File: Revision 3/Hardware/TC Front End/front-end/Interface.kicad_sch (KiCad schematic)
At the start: 18 parts, among them J1 Conn_01x02, J2 4DB-P108-02, J5 Conn_01x04, U1 LM321, U2 LM321, U3 DS18B20+

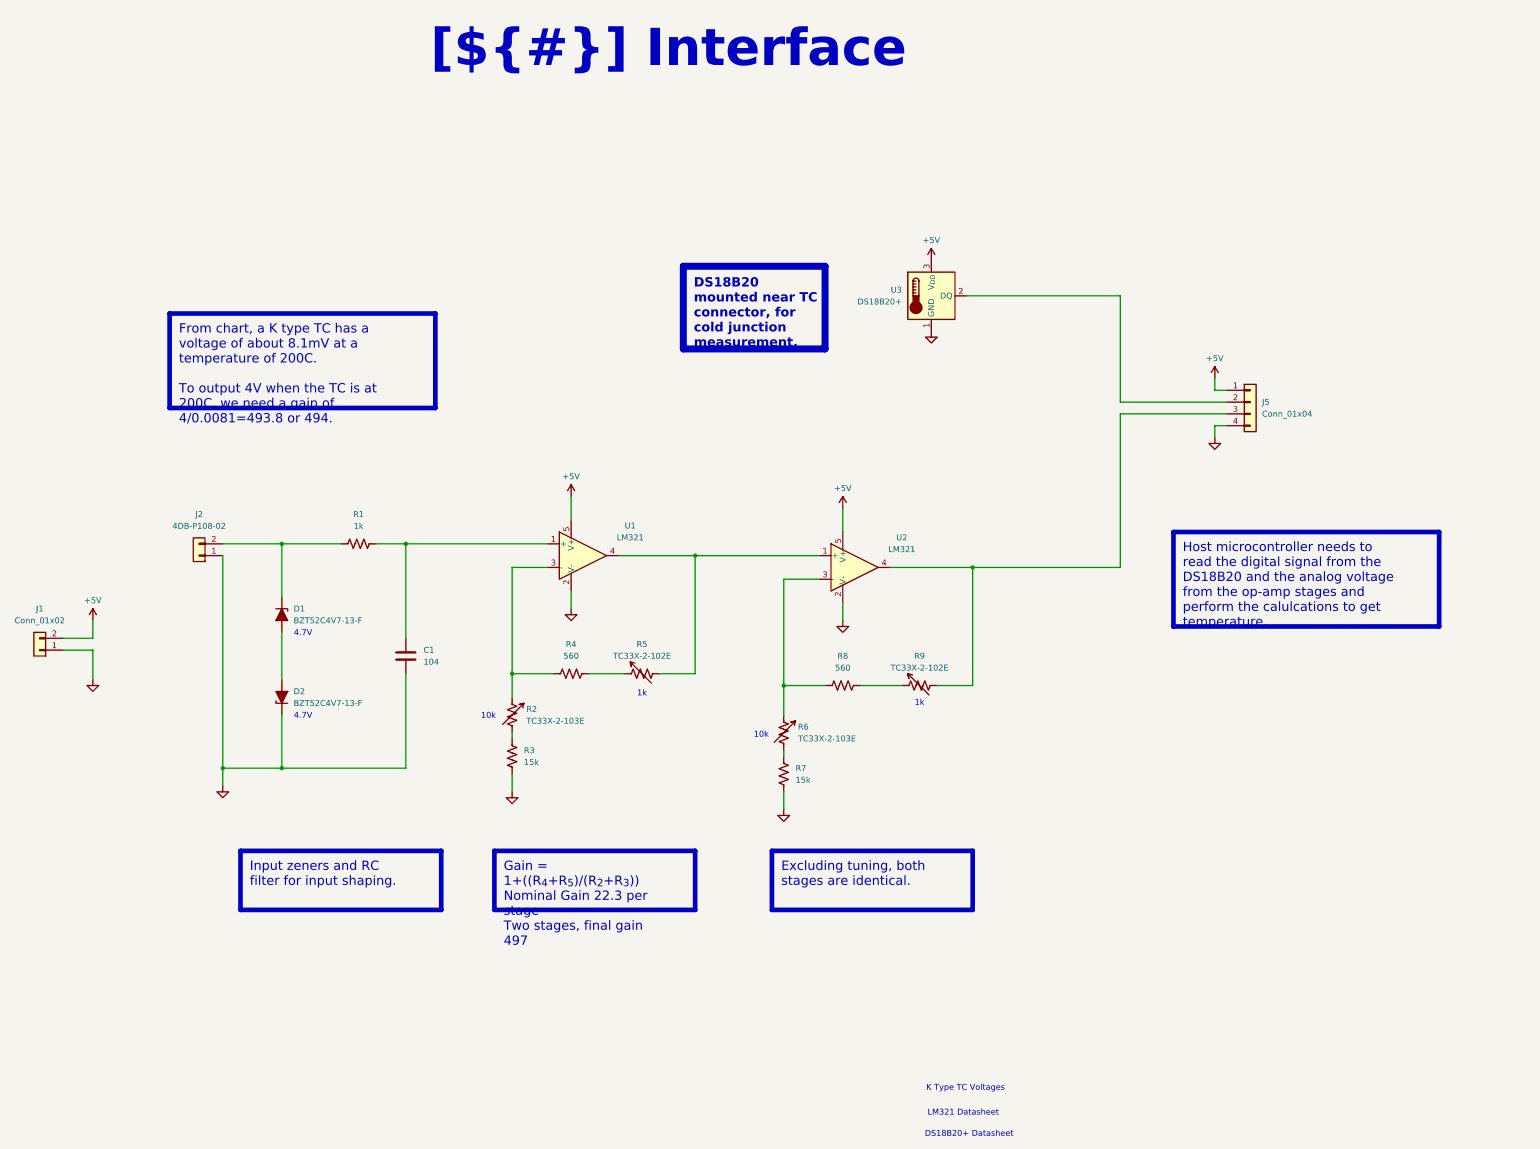
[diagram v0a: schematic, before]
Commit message: PCB layout complete, ready for routing
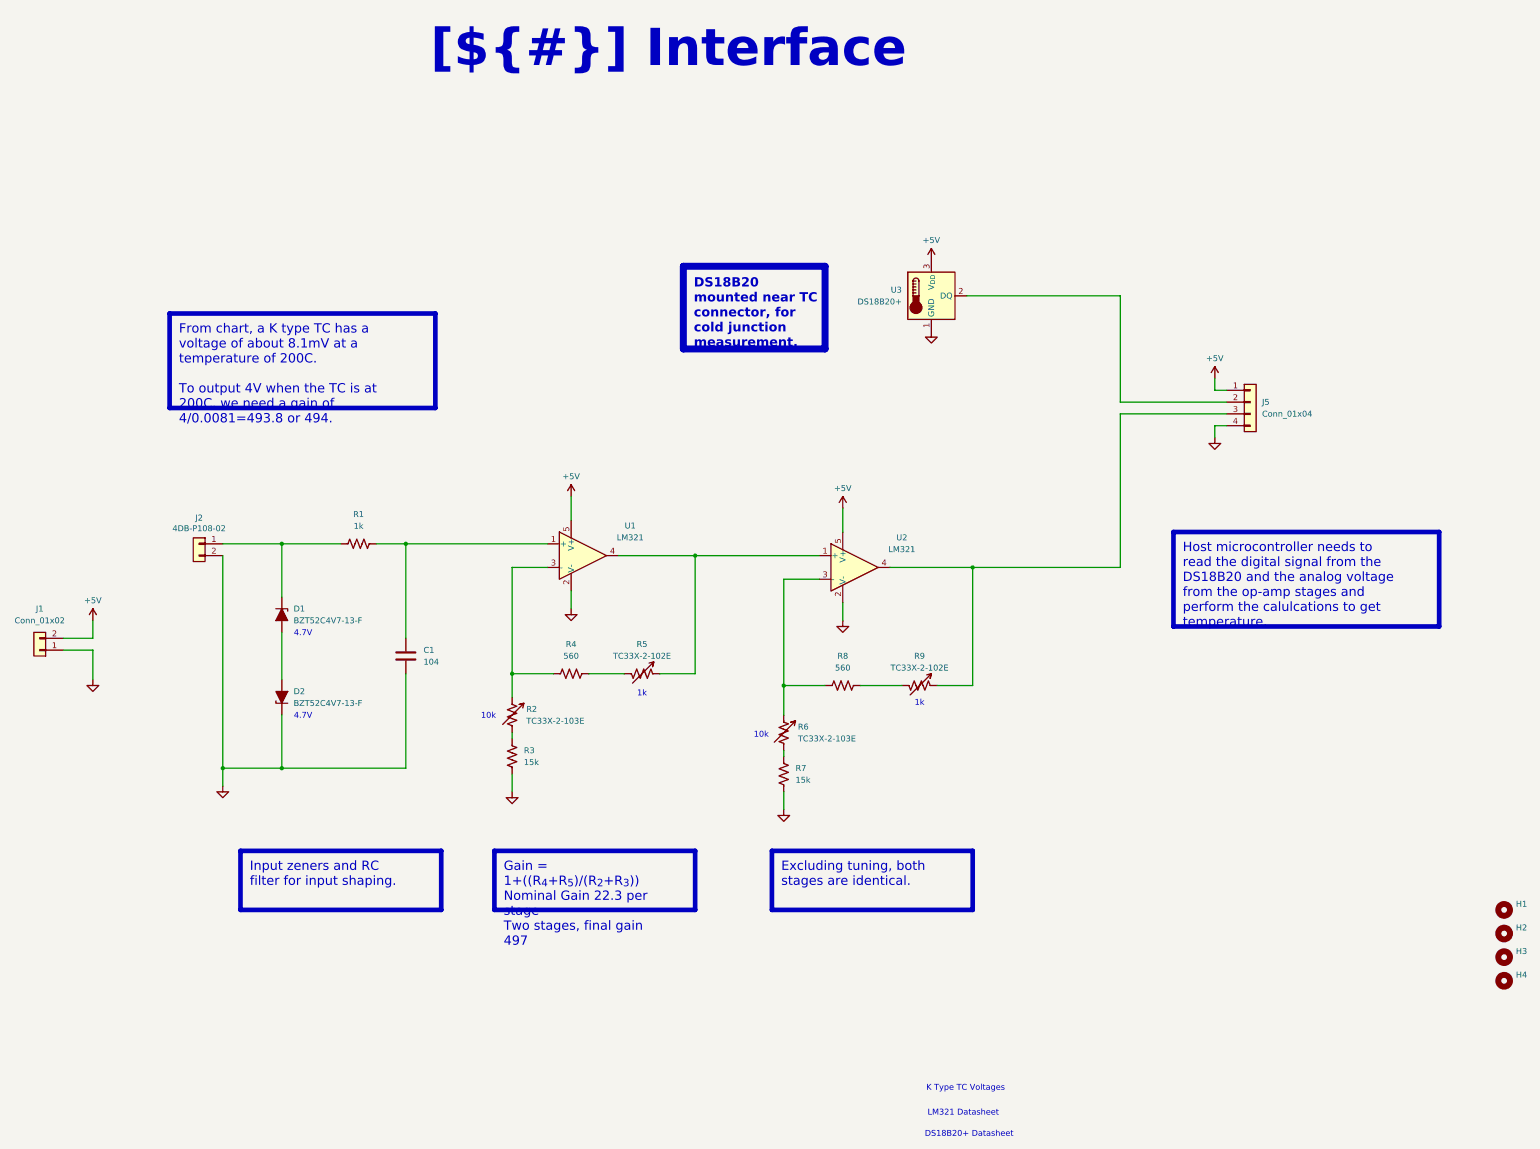
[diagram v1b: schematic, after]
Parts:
- added H1, H2, H3, H4: MountingHole, MountingHole:MountingHole_3.2mm_M3, symbol Mechanical:MountingHole
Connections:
- net GND: now also J2.2 (Pin_2); no longer J2.1 (Pin_1)
- net at R8.2: now also R9.2; no longer R9.1
- net at J5.3 (Pin_3), U2.4: now also R9.1; no longer R9.2
- net at D1.1 (K), R1.1: now also J2.1 (Pin_1); no longer J2.2 (Pin_2)
- net at R5.1: now also U1.4, U2.1 (+); no longer R4.2
- new net: R4.2, R5.2
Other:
- moved on the sheet: J2, R5, R9

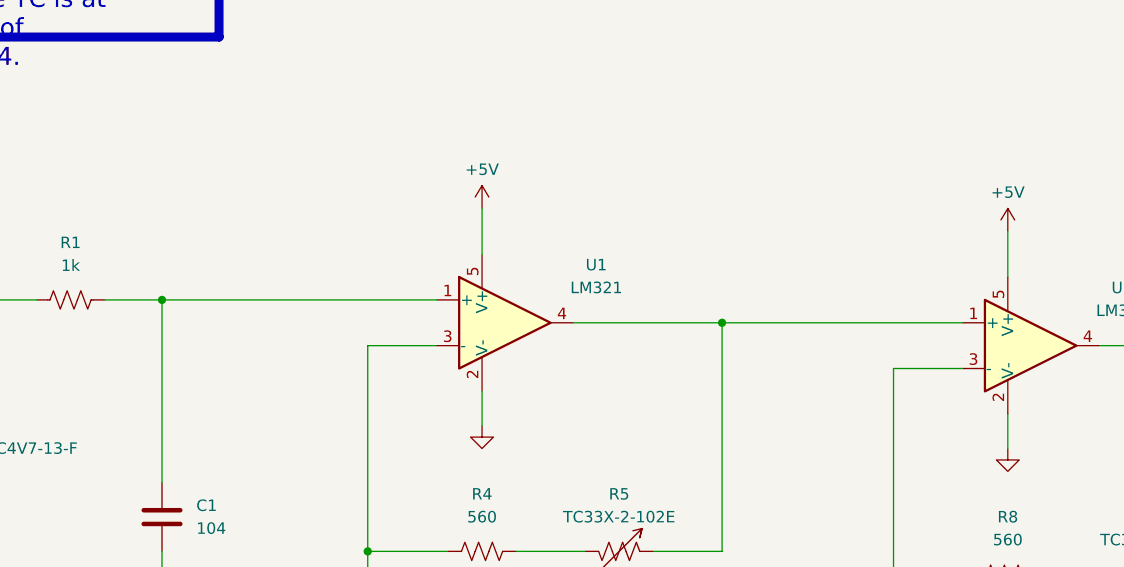
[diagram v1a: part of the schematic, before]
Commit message: Add test points for inter stages
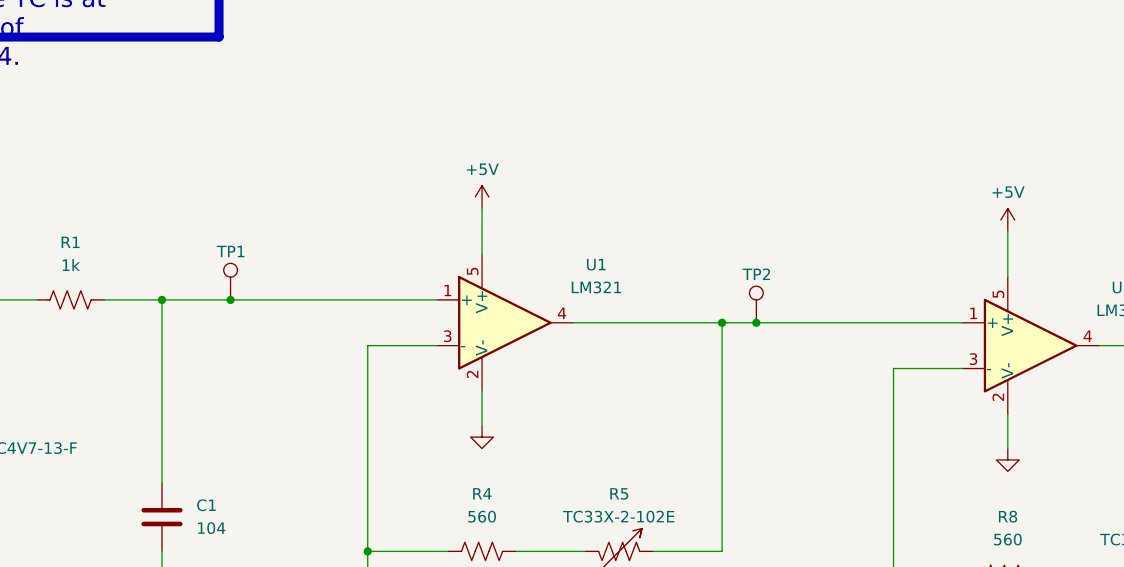
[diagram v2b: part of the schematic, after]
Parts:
- added TP1, TP2: TestPoint, TestPoint:TestPoint_THTPad_D2.0mm_Drill1.0mm, symbol Connector:TestPoint
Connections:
- net at C1.1, R1.2, U1.1 (+): now also TP1.1
- net at R5.1, U1.4, U2.1 (+): now also TP2.1
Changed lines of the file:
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@@
+	)
+	(junction
+		(at 219.71 135.89)
+		(diameter 0)
+		(color 0 0 0 0)
 	)
 	(junction
@@
 	)
 	(junction
+		(at 161.29 133.35)
+		(diameter 0)
+		(color 0 0 0 0)
+	)
+	(junction
 		(at 127 133.35)
 		(diameter 0)
@@
 	(wire
 		(pts
+			(xy 161.29 133.35) (xy 184.15 133.35)
+		)
+		(stroke
+			(width 0)
+			(type default)
+		)
+	)
+	(wire
+		(pts
 			(xy 242.57 140.97) (xy 234.95 140.97)
 		)
@@
 	(wire
 		(pts
-			(xy 153.67 133.35) (xy 184.15 133.35)
+			(xy 219.71 135.89) (xy 242.57 135.89)
+		)
+		(stroke
+			(width 0)
+			(type default)
+		)
+	)
+	(wire
+		(pts
+			(xy 153.67 133.35) (xy 161.29 133.35)
 		)
 		(stroke
@@
 	(wire
 		(pts
-			(xy 215.9 135.89) (xy 242.57 135.89)
+			(xy 215.9 135.89) (xy 219.71 135.89)
 		)
 		(stroke
@@
 	)
 	(symbol
+		(lib_id "Connector:TestPoint")
+		(at 161.29 133.35 0)
+		(unit 1)
+		(exclude_from_sim no)
+		(in_bom yes)
+		(on_board yes)
+		(dnp no)
+		(property "Reference" "TP1"
+			(at 159.766 128.016 0)
+			(effects
+				(font
+					(size 1.27 1.27)
+				)
+				(justify left)
+			)
+		)
+		(property "Value" "TestPoint"
+			(at 163.83 131.3179 0)
+			(effects
+				(font
+					(size 1.27 1.27)
+				)
+				(justify left)
+				(hide yes)
+			)
+		)
+		(property "Footprint" "TestPoint:TestPoint_THTPad_D2.0mm_Drill1.0mm"
+			(at 166.37 133.35 0)
+			(effects
+				(font
+					(size 1.27 1.27)
+				)
+				(hide yes)
+			)
+		)
+		(property "Datasheet" "~"
+			(at 166.37 133.35 0)
+			(effects
+				(font
+					(size 1.27 1.27)
+				)
+				(hide yes)
+			)
+		)
+		(property "Description" "test point"
+			(at 161.29 133.35 0)
+			(effects
+				(font
+					(size 1.27 1.27)
+				)
+				(hide yes)
+			)
+		)
+		(pin "1"
+		)
+		(instances
+			(project ""
+				(path "/0650c7a8-acba-429c-9f8e-eec0baf0bc1c/fede4c36-00cc-4d3d-b71c-5243ba232202"
+					(reference "TP1")
+					(unit 1)
+				)
+			)
+		)
+	)
+	(symbol
 		(lib_id "power:+5V")
 		(at 86.36 149.86 0)
@@
 					(unit 1)
 				)
+			)
+		)
+	)
+	(symbol
+		(lib_id "Connector:TestPoint")
+		(at 219.71 135.89 0)
+		(unit 1)
+		(exclude_from_sim no)
+		(in_bom yes)
+		(on_board yes)
+		(dnp no)
+		(property "Reference" "TP2"
+			(at 218.186 130.556 0)
+			(effects
+				(font
+					(size 1.27 1.27)
+				)
+				(justify left)
+			)
+		)
+		(property "Value" "TestPoint"
+			(at 222.25 133.8579 0)
+			(effects
+				(font
+					(size 1.27 1.27)
+				)
+				(justify left)
+				(hide yes)
+			)
+		)
+		(property "Footprint" "TestPoint:TestPoint_THTPad_D2.0mm_Drill1.0mm"
+			(at 224.79 135.89 0)
+			(effects
+				(font
+					(size 1.27 1.27)
+				)
+				(hide yes)
+			)
+		)
+		(property "Datasheet" "~"
+			(at 224.79 135.89 0)
+			(effects
+				(font
+					(size 1.27 1.27)
+				)
+				(hide yes)
+			)
+		)
+		(property "Description" "test point"
+			(at 219.71 135.89 0)
+			(effects
+				(font
+					(size 1.27 1.27)
+				)
+				(hide yes)
+			)
+		)
+		(pin "1"
+		)
+		(instances
+			(project "front-end"
+				(path "/0650c7a8-acba-429c-9f8e-eec0baf0bc1c/fede4c36-00cc-4d3d-b71c-5243ba232202"
+					(reference "TP2")
+					(unit 1)
+				)
